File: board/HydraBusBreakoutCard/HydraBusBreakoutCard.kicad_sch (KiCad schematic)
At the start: 11 parts, among them J1 Bus_Hydra_8bit, J10 I2C, J11 Power, J2 Data Bus, J3 Address Bus, J4 SPI, J5 Interrupts & I/O, J6 Clocks, J7 Bus Control, J8 Reset, J9 Audio

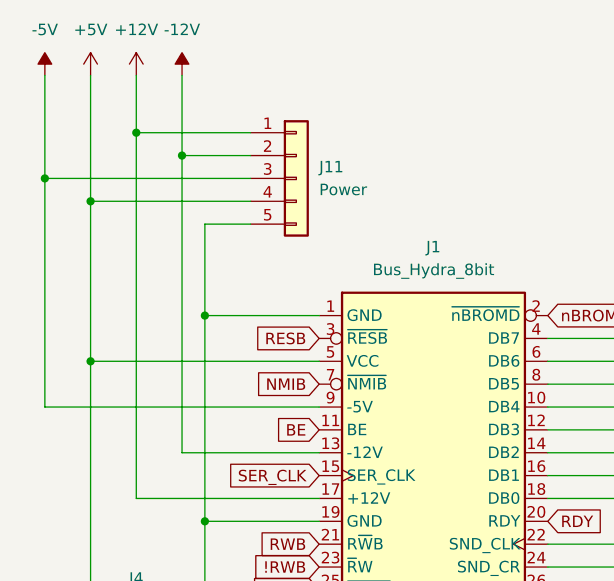
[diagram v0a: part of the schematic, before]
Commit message: Board version 0.6F, moving stuff around and updating the silkscreen to be more consistent.
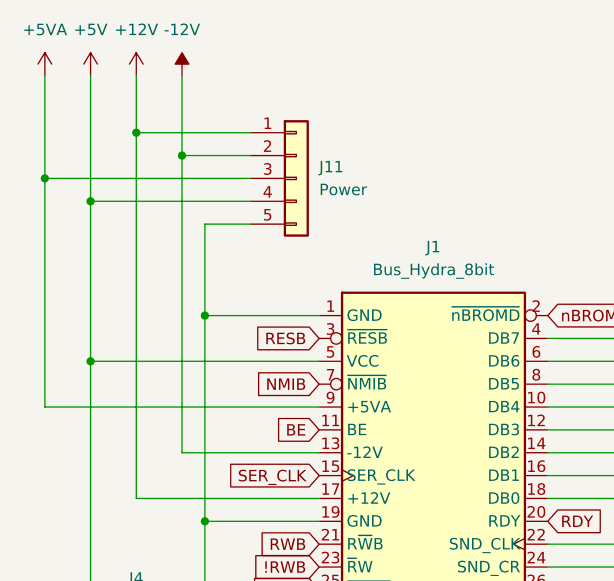
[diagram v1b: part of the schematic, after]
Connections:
- net -5V renamed +5VA
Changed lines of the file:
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@@
 	)
 	(symbol
-		(lib_id "power:-5V")
+		(lib_id "power:+5VA")
 		(at 58.42 24.13 0)
 		(unit 1)
@@
 			)
 		)
-		(property "Value" "-5V"
+		(property "Value" "+5VA"
 			(at 58.42 19.05 0)
 			(effects
@@
 			)
 		)
-		(property "Description" "Power symbol creates a global label with name \"-5V\""
+		(property "Description" "Power symbol creates a global label with name \"+5VA\""
 			(at 58.42 24.13 0)
 			(effects

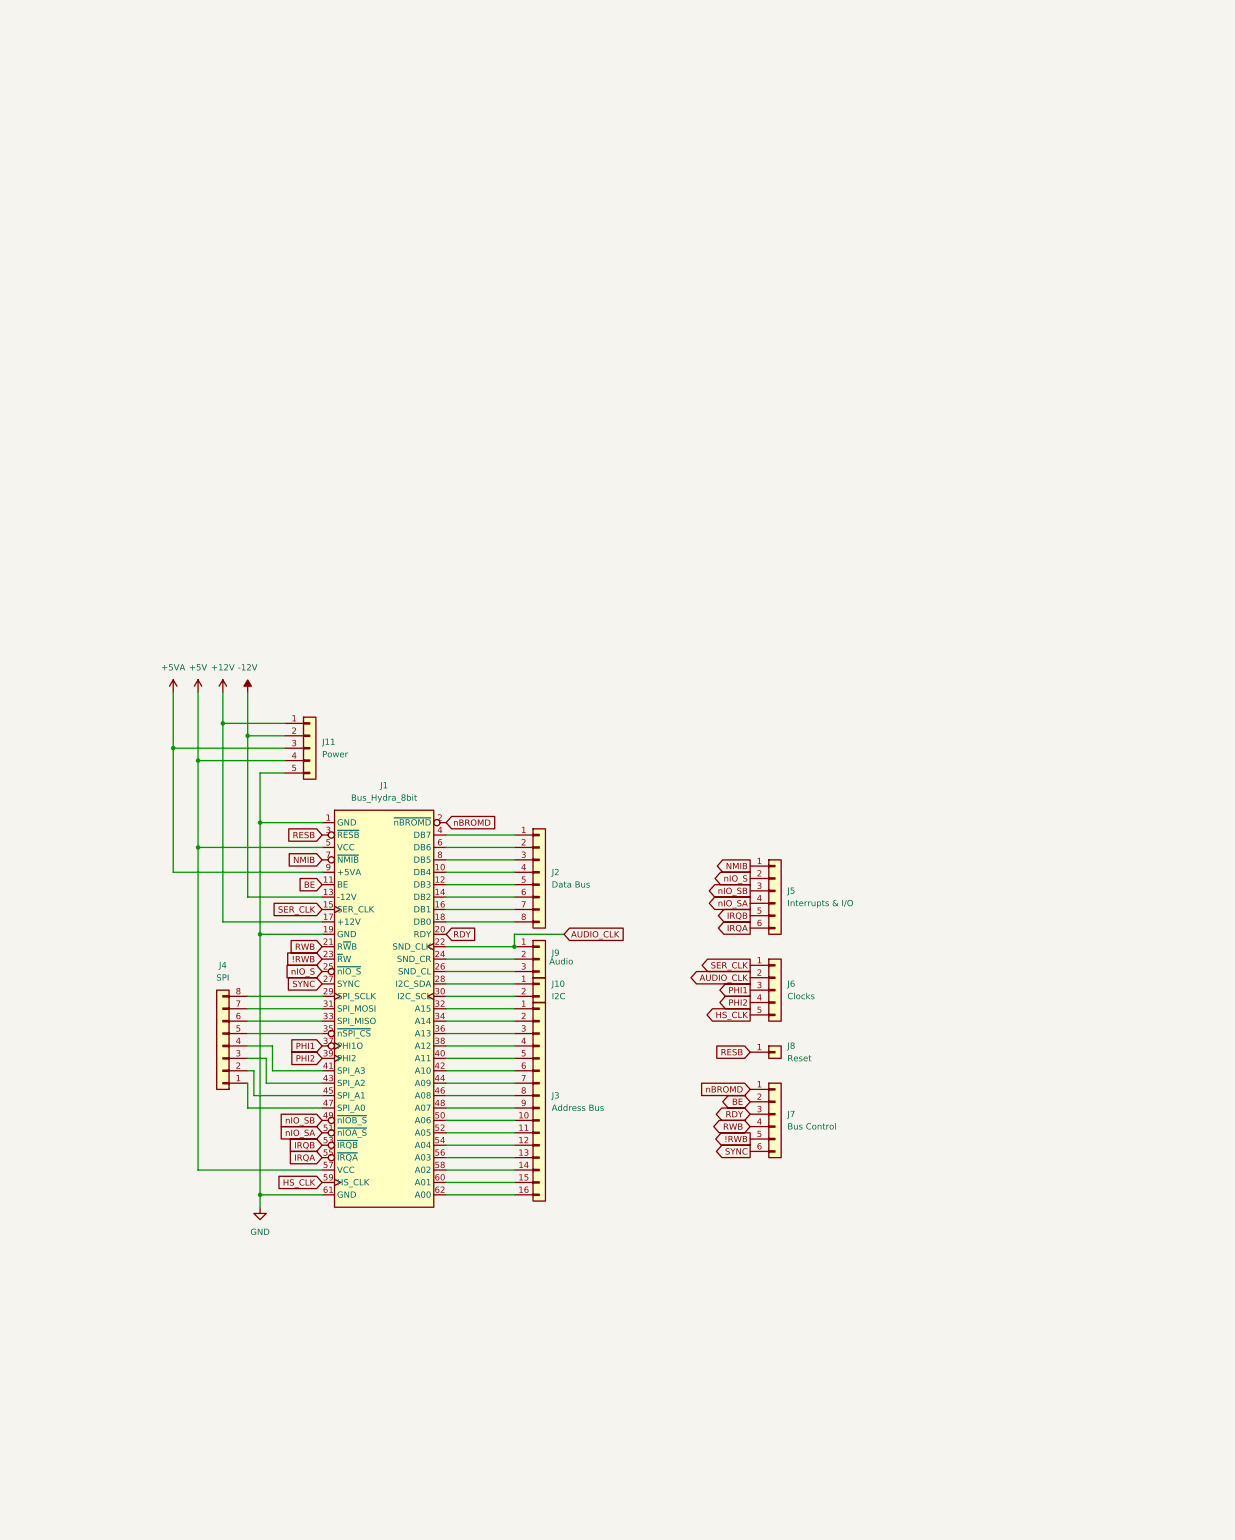
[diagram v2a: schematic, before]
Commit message: V2.0 updates and new hydra breakout and counter cards.
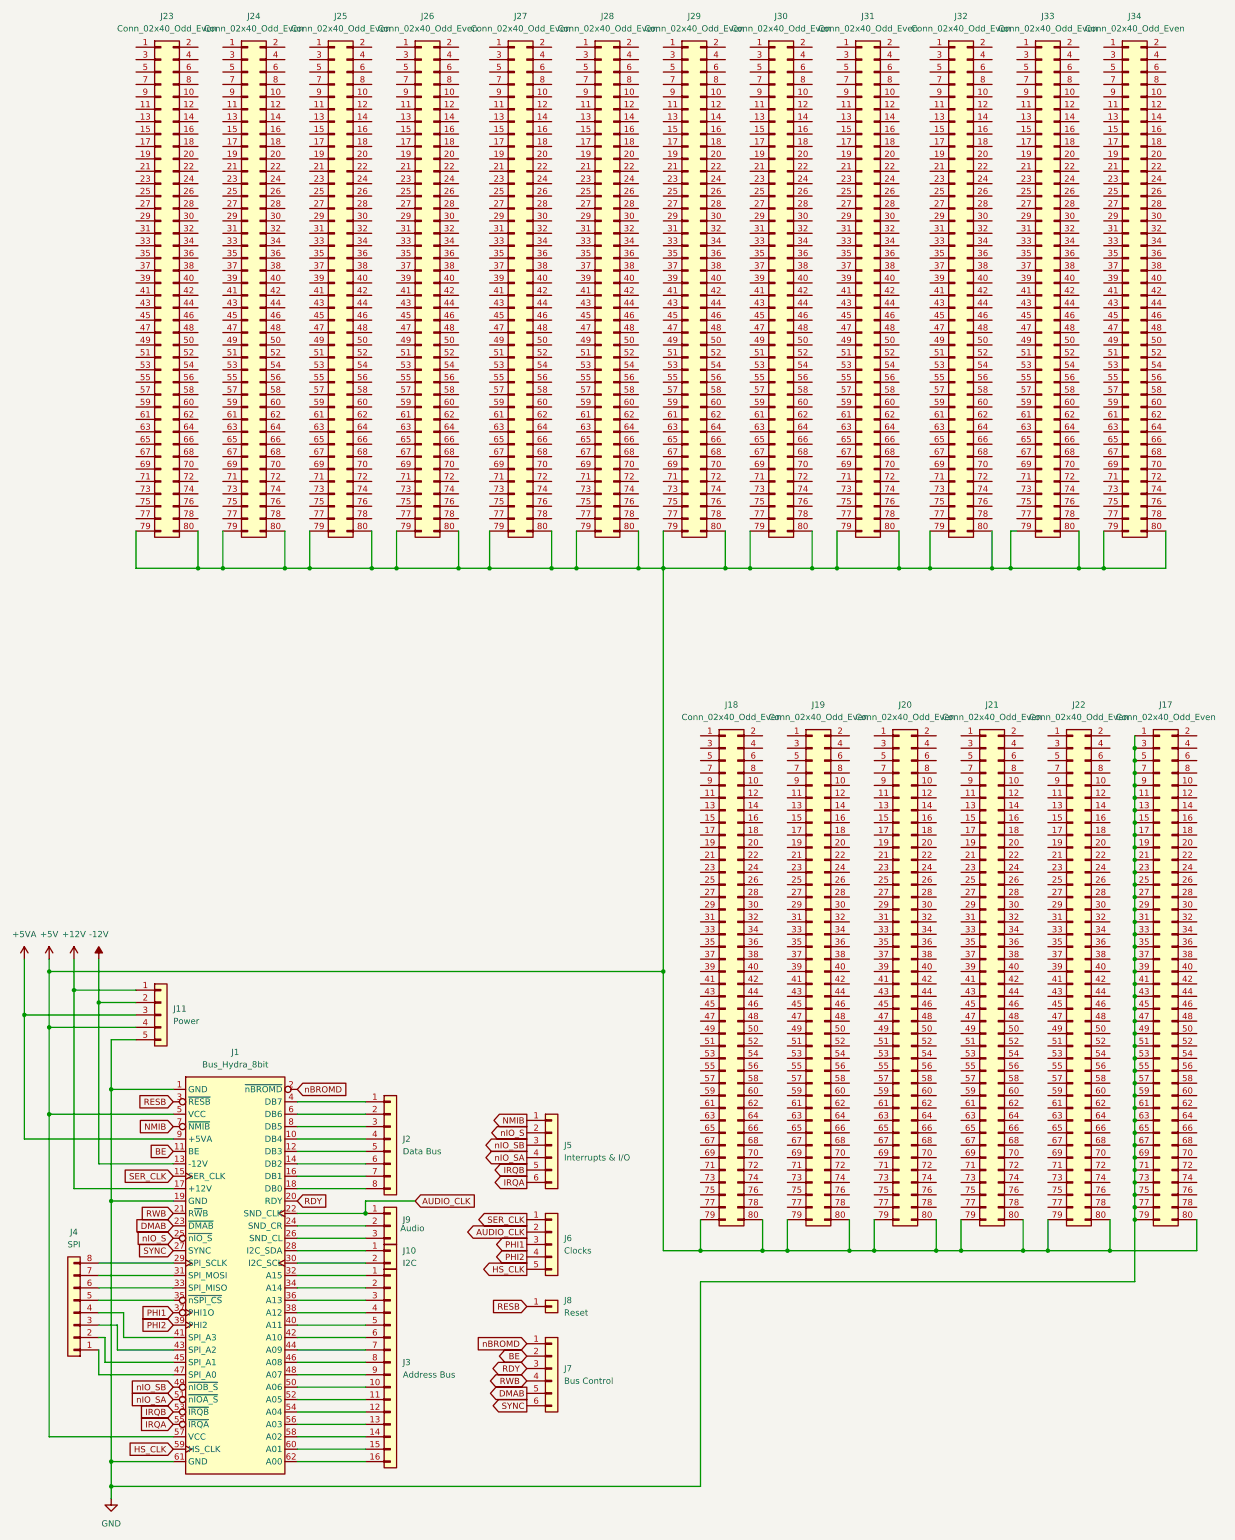
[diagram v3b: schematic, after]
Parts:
- added J17, J18, J19, J20, J21, J22, J23, J24, J25, J26, J27, J28, J29, J30, J31, J32, J33, J34: Conn_02x40_Odd_Even, Connector_PinHeader_2.54mm:PinHeader_2x40_P2.54mm_Vertical, symbol Connector_Generic:Conn_02x40_Odd_Even
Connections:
- net +5V: now also J17.80 (Pin_80), J18.79 (Pin_79), J18.80 (Pin_80), J19.79 (Pin_79), J19.80 (Pin_80), J20.79 (Pin_79), J20.80 (Pin_80), J21.79 (Pin_79), J21.80 (Pin_80), J22.79 (Pin_79), J22.80 (Pin_80), J23.79 (Pin_79), J23.80 (Pin_80), J24.79 (Pin_79), J24.80 (Pin_80), J25.79 (Pin_79), J25.80 (Pin_80), J26.79 (Pin_79), J26.80 (Pin_80), J27.79 (Pin_79), J27.80 (Pin_80), J28.79 (Pin_79), J28.80 (Pin_80), J29.79 (Pin_79), J29.80 (Pin_80), J30.79 (Pin_79), J30.80 (Pin_80), J31.79 (Pin_79), J31.80 (Pin_80), J32.79 (Pin_79), J32.80 (Pin_80), J33.79 (Pin_79), J33.80 (Pin_80), J34.79 (Pin_79), J34.80 (Pin_80)
- net GND: now also J17.1 (Pin_1), J17.11 (Pin_11), J17.13 (Pin_13), J17.15 (Pin_15), J17.17 (Pin_17), J17.19 (Pin_19), J17.21 (Pin_21), J17.23 (Pin_23), J17.25 (Pin_25), J17.27 (Pin_27), J17.29 (Pin_29), J17.3 (Pin_3), J17.31 (Pin_31), J17.33 (Pin_33), J17.35 (Pin_35), J17.37 (Pin_37), J17.39 (Pin_39), J17.41 (Pin_41), J17.43 (Pin_43), J17.45 (Pin_45), J17.47 (Pin_47), J17.49 (Pin_49), J17.5 (Pin_5), J17.51 (Pin_51), J17.53 (Pin_53), J17.55 (Pin_55), J17.57 (Pin_57), J17.59 (Pin_59), J17.61 (Pin_61), J17.63 (Pin_63), J17.65 (Pin_65), J17.67 (Pin_67), J17.69 (Pin_69), J17.7 (Pin_7), J17.71 (Pin_71), J17.73 (Pin_73), J17.75 (Pin_75), J17.77 (Pin_77), J17.79 (Pin_79), J17.9 (Pin_9)
- net !RWB renamed DMAB
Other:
- moved on the sheet: J1, J10, J11, J2, J3, J4, J5, J6, J7, J8, J9
